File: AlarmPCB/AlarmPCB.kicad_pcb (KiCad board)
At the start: 2 copper layers, 99.9 x 74 mm, 17 parts

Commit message: PCB revisions
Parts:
- moved PB2 13.8 mm to (160.7, 158.0)
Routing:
- net /D3: track 17.0 -> 47.8 mm
- net /D11: track 12.9 -> 43.8 mm
- net /D10: track 13.9 -> 44.8 mm
- net Net-(DS1-Pad9): track 0.00 -> 30.9 mm
- net Net-(DS1-Pad8): track 0.00 -> 30.9 mm
- net Net-(DS1-Pad7): track 0.00 -> 30.9 mm
- net Net-(DS1-Pad3): track 22.6 -> 53.4 mm
- net Net-(DS1-Pad16): track 31.6 -> 62.4 mm
- net Net-(DS1-Pad10): track 0.00 -> 30.9 mm
- net /D5: track 17.0 -> 47.8 mm
- net /D4: track 17.0 -> 47.8 mm
- net /D12: track 15.5 -> 46.3 mm
- net /D2: track 17.0 -> 47.8 mm
- net /A1: track 0.00 -> 19.3 mm
- net /A2: track 19.1 -> 30.1 mm
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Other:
- board text added: "G01_B03"

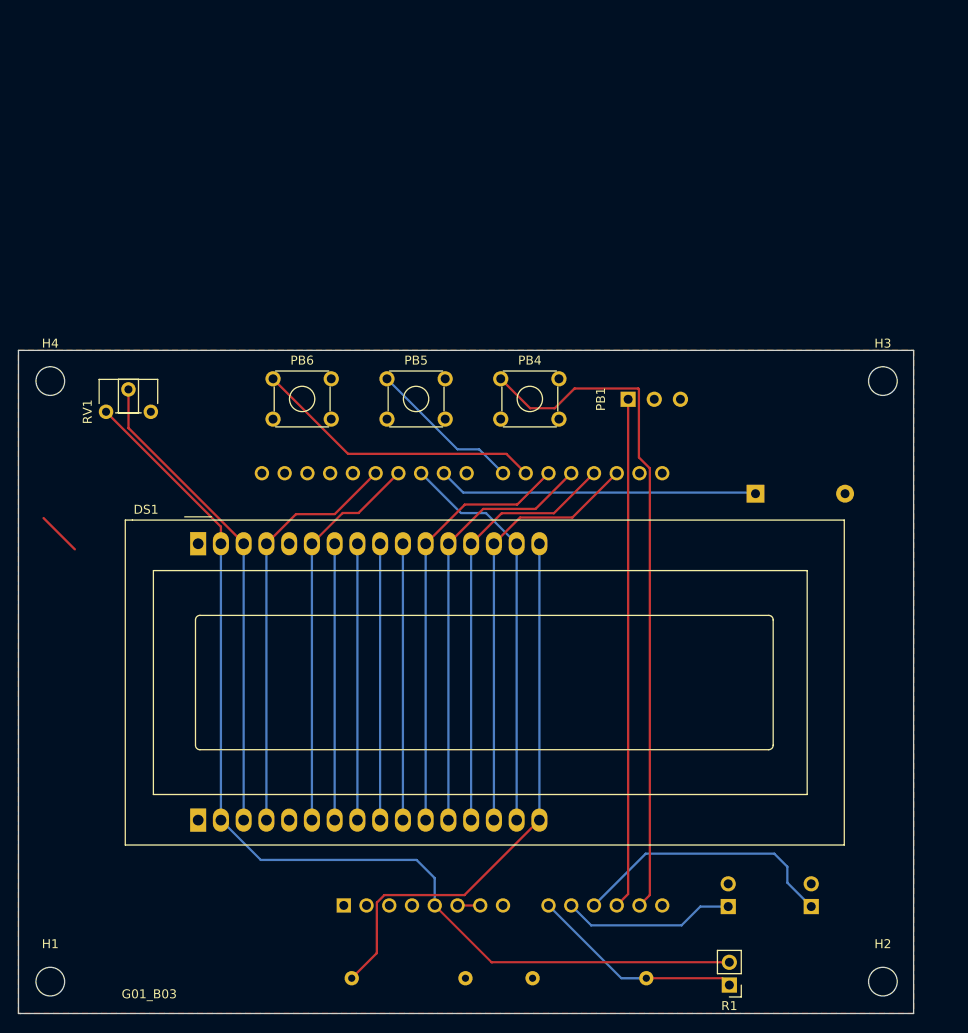
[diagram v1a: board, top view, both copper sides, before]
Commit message: Updated Pot footprint
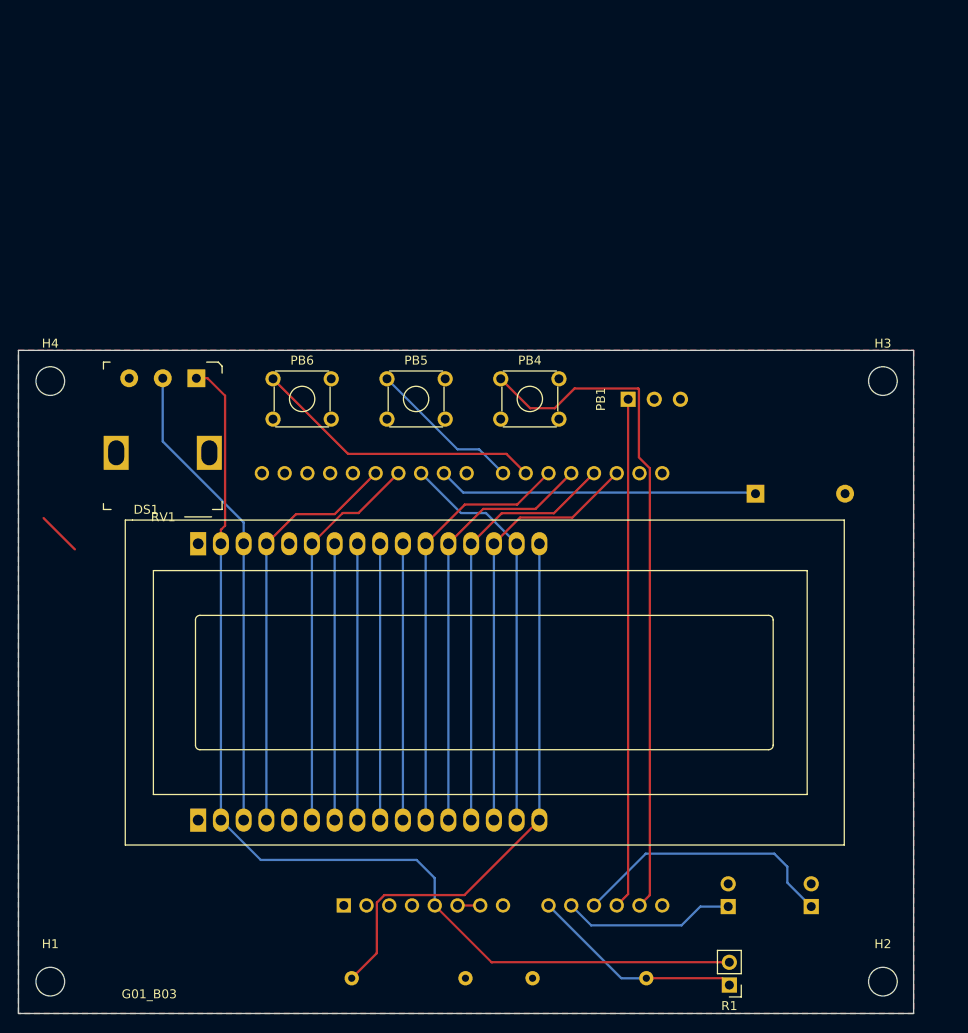
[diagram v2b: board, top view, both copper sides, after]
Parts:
- RV1: footprint Potentiometer_THT:Potentiometer_ACP_CA6-H2,5_Horizontal -> digikey-footprints:Potentiometer_P120PK-Y25BR10K
- moved RV1 10.8 mm to (92.0, 99.0), turned to 180 degrees
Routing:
- net +5V: track 116.0 -> 116.7 mm
- added copper zone on B.Cu, net GND
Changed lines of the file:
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@@
-(kicad_pcb (version 20171130) (host pcbnew "(5.1.6)-1")
+(kicad_pcb (version 20171130) (host pcbnew "(5.1.4)-1")
   (general
     (thickness 1.6)
     (drawings 22)
-    (tracks 86)
+    (tracks 89)
     (zones 0)
     (modules 17)
@@
   (page A4)
   (layers
-    (0 F.Cu signal hide)
+    (0 F.Cu signal)
     (31 B.Cu signal)
     (32 B.Adhes user)
@@
     (add_net "Net-(DS1-Pad9)")
   )
+  (module digikey-footprints:Potentiometer_P120PK-Y25BR10K (layer F.Cu)
+    (at 92 99 180)
+    (fp_text reference RV1 (at 3.7 -15.5) (layer F.SilkS)
+      (effects (font (size 1 1) (thickness 0.15)))
+    )
+    (fp_text value Contrast (at 3.625 2.8) (layer F.Fab)
+      (effects (font (size 1 1) (thickness 0.15)))
+    )
+    (fp_line (start -2.75 -14.525) (end 10.25 -14.525) (layer F.Fab) (width 0.1))
+    (fp_line (start 10.25 -14.525) (end 10.25 1.675) (layer F.Fab) (width 0.1))
+    (fp_line (start -2.75 1.275) (end -2.375 1.675) (layer F.Fab) (width 0.1))
+    (fp_line (start -2.375 1.675) (end 10.25 1.675) (layer F.Fab) (width 0.1))
+    (fp_line (start -2.75 1.275) (end -2.75 -14.525) (layer F.Fab) (width 0.1))
+    (fp_line (start 10.375 -14.65) (end 10.375 -14) (layer F.SilkS) (width 0.1))
+    (fp_line (start 9.525 -14.65) (end 10.375 -14.65) (layer F.SilkS) (width 0.1))
+    (fp_line (start 10.375 1.8) (end 9.625 1.8) (layer F.SilkS) (width 0.1))
+    (fp_line (start 10.375 1.025) (end 10.375 1.8) (layer F.SilkS) (width 0.1))
+    (fp_line (start -2.875 -14.65) (end -2.875 -13.75) (layer F.SilkS) (width 0.1))
+    (fp_line (start -1.8 -14.65) (end -2.875 -14.65) (layer F.SilkS) (width 0.1))
+    (fp_line (start -2.45 1.8) (end -1.15 1.8) (layer F.SilkS) (width 0.1))
+    (fp_line (start -2.875 1.35) (end -2.45 1.8) (layer F.SilkS) (width 0.1))
+    (fp_line (start -2.875 0.575) (end -2.875 1.35) (layer F.SilkS) (width 0.1))
+    (fp_text user %R (at 4.05 -6.65) (layer F.Fab)
+      (effects (font (size 1 1) (thickness 0.15)))
+    )
+    (fp_line (start -3.1 -14.825) (end 10.6 -14.825) (layer F.CrtYd) (width 0.05))
+    (fp_line (start 10.6 -14.825) (end 10.6 1.975) (layer F.CrtYd) (width 0.05))
+    (fp_line (start 10.6 1.975) (end -3.1 1.975) (layer F.CrtYd) (width 0.05))
+    (fp_line (start -3.1 1.975) (end -3.1 -14.825) (layer F.CrtYd) (width 0.05))
+    (pad 4 thru_hole rect (at 8.95 -8.325 180) (size 2.8 3.8) (drill oval 1.8 2.8) (layers *.Cu *.Mask))
+    (pad 4 thru_hole rect (at -1.45 -8.325 180) (size 2.8 3.8) (drill oval 1.8 2.8) (layers *.Cu *.Mask))
+    (pad 3 thru_hole circle (at 7.5 0 180) (size 2 2) (drill 1) (layers *.Cu *.Mask)
+      (net 5 GND))
+    (pad 2 thru_hole circle (at 3.75 0 180) (size 2 2) (drill 1) (layers *.Cu *.Mask)
+      (net 36 "Net-(DS1-Pad3)"))
+    (pad 1 thru_hole rect (at 0 0 180) (size 2 2) (drill 1) (layers *.Cu *.Mask)
+      (net 20 +5V))
+  )
   (module Display:WC1602A (layer F.Cu)
     (at 92.202 117.475)
@@
     )
   )
-  (module Potentiometer_THT:Potentiometer_ACP_CA6-H2,5_Horizontal (layer F.Cu)
-    (at 81.915 102.743 90)
-    (descr "Potentiometer, horizontal, ACP CA6-H2,5, http://www.acptechnologies.com/wp-content/uploads/2017/06/01-ACP-CA6.pdf")
-    (tags "Potentiometer horizontal ACP CA6-H2,5")
-    (fp_text reference RV1 (at 0 -2.06 90) (layer F.SilkS)
-      (effects (font (size 1 1) (thickness 0.15)))
-    )
-    (fp_text value Contrast (at 0 7.06 90) (layer F.Fab)
-      (effects (font (size 1 1) (thickness 0.15)))
-    )
-    (fp_line (start 3.75 -1.1) (end -1.1 -1.1) (layer F.CrtYd) (width 0.05))
-    (fp_line (start 3.75 6.1) (end 3.75 -1.1) (layer F.CrtYd) (width 0.05))
-    (fp_line (start -1.1 6.1) (end 3.75 6.1) (layer F.CrtYd) (width 0.05))
-    (fp_line (start -1.1 -1.1) (end -1.1 6.1) (layer F.CrtYd) (width 0.05))
-    (fp_line (start 3.62 1.38) (end 3.62 3.62) (layer F.SilkS) (width 0.12))
-    (fp_line (start -0.121 1.38) (end -0.121 3.62) (layer F.SilkS) (width 0.12))
-    (fp_line (start -0.121 3.62) (end 3.62 3.62) (layer F.SilkS) (width 0.12))
-    (fp_line (start -0.121 1.38) (end 3.62 1.38) (layer F.SilkS) (width 0.12))
-    (fp_line (start -0.121 1.066) (end -0.121 3.935) (layer F.SilkS) (width 0.12))
-    (fp_line (start 3.62 -0.77) (end 3.62 5.77) (layer F.SilkS) (width 0.12))
-    (fp_line (start 0.925 5.77) (end 3.62 5.77) (layer F.SilkS) (width 0.12))
-    (fp_line (start 0.925 -0.77) (end 3.62 -0.77) (layer F.SilkS) (width 0.12))
-    (fp_line (start 3.5 1.5) (end 0 1.5) (layer F.Fab) (width 0.1))
-    (fp_line (start 3.5 3.5) (end 3.5 1.5) (layer F.Fab) (width 0.1))
-    (fp_line (start 0 3.5) (end 3.5 3.5) (layer F.Fab) (width 0.1))
-    (fp_line (start 0 1.5) (end 0 3.5) (layer F.Fab) (width 0.1))
-    (fp_line (start 0 -0.65) (end 3.5 -0.65) (layer F.Fab) (width 0.1))
-    (fp_line (start 0 5.65) (end 0 -0.65) (layer F.Fab) (width 0.1))
-    (fp_line (start 3.5 5.65) (end 0 5.65) (layer F.Fab) (width 0.1))
-    (fp_line (start 3.5 -0.65) (end 3.5 5.65) (layer F.Fab) (width 0.1))
-    (fp_text user %R (at 1.75 2.5 90) (layer F.Fab)
-      (effects (font (size 0.78 0.78) (thickness 0.15)))
-    )
-    (pad 1 thru_hole circle (at 0 0 90) (size 1.62 1.62) (drill 0.9) (layers *.Cu *.Mask)
-      (net 20 +5V))
-    (pad 2 thru_hole circle (at 2.5 2.5 90) (size 1.62 1.62) (drill 0.9) (layers *.Cu *.Mask)
-      (net 36 "Net-(DS1-Pad3)"))
-    (pad 3 thru_hole circle (at 0 5 90) (size 1.62 1.62) (drill 0.9) (layers *.Cu *.Mask)
-      (net 5 GND))
-    (model ${KISYS3DMOD}/Potentiometer_THT.3dshapes/Potentiometer_ACP_CA6-H2,5_Horizontal.wrl
-      (at (xyz 0 0 0))
-      (scale (xyz 1 1 1))
-      (rotate (xyz 0 0 0))
-    )
-  )
   (module Resistor_THT:R_Axial_DIN0309_L9.0mm_D3.2mm_P12.70mm_Horizontal (layer B.Cu)
     (at 129.54 165.989)
@@
   (segment (start 126.619 107.442) (end 128.778 109.601) (width 0.254) (layer F.Cu) (net 19))
   (segment (start 108.943 107.442) (end 126.619 107.442) (width 0.254) (layer F.Cu) (net 19))
-  (segment (start 94.742 115.57) (end 94.742 117.475) (width 0.254) (layer F.Cu) (net 20))
-  (segment (start 81.915 102.743) (end 94.742 115.57) (width 0.254) (layer F.Cu) (net 20))
   (segment (start 124.968 164.211) (end 151.511 164.211) (width 0.254) (layer F.Cu) (net 20))
   (segment (start 118.618 157.861) (end 124.968 164.211) (width 0.254) (layer F.Cu) (net 20))
@@
   (segment (start 99.187 152.781) (end 94.742 148.336) (width 0.254) (layer B.Cu) (net 20))
   (segment (start 116.586 152.781) (end 99.187 152.781) (width 0.254) (layer B.Cu) (net 20))
+  (segment (start 94.742 115.921) (end 94.742 117.475) (width 0.254) (layer F.Cu) (net 20))
+  (segment (start 95.205601 115.457399) (end 94.742 115.921) (width 0.254) (layer F.Cu) (net 20))
+  (segment (start 95.205601 100.951601) (end 95.205601 115.457399) (width 0.254) (layer F.Cu) (net 20))
+  (segment (start 93.254 99) (end 95.205601 100.951601) (width 0.254) (layer F.Cu) (net 20))
+  (segment (start 92 99) (end 93.254 99) (width 0.254) (layer F.Cu) (net 20))
   (segment (start 121.97083 113.10617) (end 117.602 117.475) (width 0.254) (layer F.Cu) (net 21))
   (segment (start 127.81283 113.10617) (end 121.97083 113.10617) (width 0.254) (layer F.Cu) (net 21))
@@
   (segment (start 109.982 117.475) (end 109.982 148.336) (width 0.254) (layer B.Cu) (net 34))
   (segment (start 107.442 117.475) (end 107.442 148.336) (width 0.254) (layer B.Cu) (net 35))
-  (segment (start 97.282 117.427488) (end 97.282 117.475) (width 0.254) (layer F.Cu) (net 36))
-  (segment (start 84.415 104.560488) (end 97.282 117.427488) (width 0.254) (layer F.Cu) (net 36))
-  (segment (start 84.415 100.243) (end 84.415 104.560488) (width 0.254) (layer F.Cu) (net 36))
   (segment (start 97.282 117.475) (end 97.282 148.336) (width 0.254) (layer B.Cu) (net 36))
+  (segment (start 97.282 115.097082) (end 97.282 117.475) (width 0.254) (layer B.Cu) (net 36))
+  (segment (start 88.25 99) (end 88.25 106.065082) (width 0.254) (layer B.Cu) (net 36))
+  (segment (start 88.25 106.065082) (end 97.282 115.097082) (width 0.254) (layer B.Cu) (net 36))
   (zone (net 5) (net_name GND) (layer F.Cu) (hatch edge 0.508)
     (connect_pads (clearance 0.508))
     (min_thickness 0.254)
+    (fill yes (arc_segments 32) (thermal_gap 0.508) (thermal_bridge_width 0.508))
+    (polygon
+      (pts
+        (xy 172.085 169.926) (xy 72.136 169.926) (xy 72.136 95.885) (xy 172.085 95.885)
+      )
+    )
+  )
+  (zone (net 5) (net_name GND) (layer B.Cu) (hatch edge 0.508)
+    (connect_pads (clearance 0.508))
+    (min_thickness 0.254)

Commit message: PCB rev
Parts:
- PB1: footprint Connector_PinHeader_2.54mm:PinHeader_1x03_P2.54mm_Vertical -> Button_Switch_THT:SW_TH_Tactile_Omron_B3F-10xx
- moved PB1 4.90 mm to (145.3, 103.7), turned to 180 degrees
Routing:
- net /A4: track 76.4 -> 68.8 mm
- net GND: track 7.49 -> 2.54 mm
- net /A3: track 57.0 -> 60.3 mm

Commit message: Final PCB
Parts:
- moved A1 20.2 mm to (88.4, 160.6)
- moved PB2 14.4 mm to (146.3, 157.7)
- moved PB3 14.4 mm to (137.0, 157.7)
- moved RV1 9.69 mm to (82.3, 98.1), turned to 270 degrees
- moved H3 1.43 mm to (168.1, 98.0)
- moved H4 1.38 mm to (76.1, 98.0)
- moved PB1 1.12 mm to (146.3, 103.2)
- moved PB4 0.92 mm to (126.8, 98.8)
- moved H2 0.67 mm to (168.1, 166.0)
- moved PB5 0.65 mm to (113.8, 98.8)
- moved H1 0.55 mm to (76.1, 166.0)
- moved PB6 0.42 mm to (100.8, 98.8)
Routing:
- net Net-(A1-Pad24): track 35.7 -> 56.0 mm
- net /D10: track 44.8 -> 63.7 mm
- net Net-(A1-Pad9): track 23.9 -> 42.8 mm
- net /D6: track 32.6 -> 16.8 mm
- net +5V: track 116.7 -> 129.7 mm
- net /A3: track 60.3 -> 71.3 mm
- net /D5: track 47.8 -> 39.3 mm
- net /D4: track 47.8 -> 39.3 mm
- net /D3: track 47.8 -> 39.3 mm
- net /D2: track 47.8 -> 39.3 mm
- net /A1: track 19.3 -> 25.7 mm
- net /D12: track 46.3 -> 40.8 mm
- net /A4: track 68.8 -> 64.8 mm, vias 0 -> 1
- net Net-(DS1-Pad3): track 53.1 -> 56.8 mm
- net /A2: track 30.1 -> 32.9 mm
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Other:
- board size 99.9 x 74 mm -> 100 x 76 mm

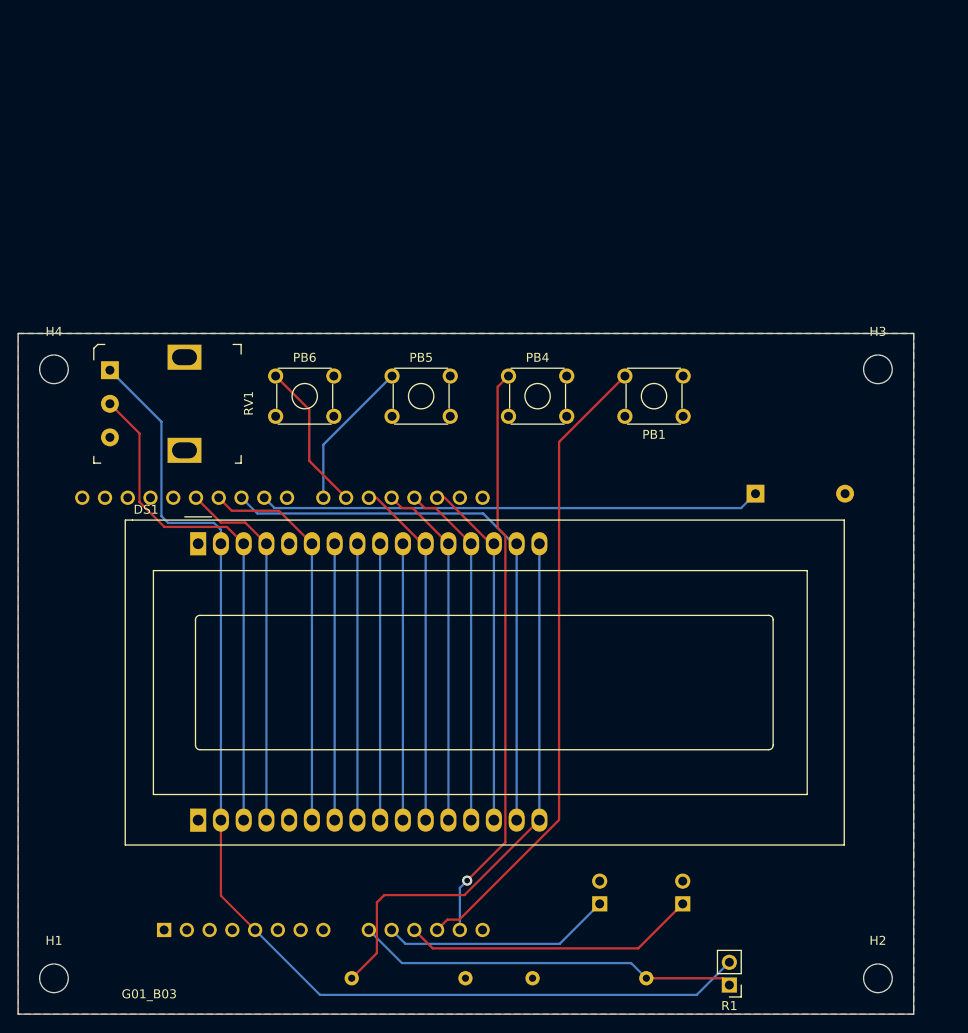
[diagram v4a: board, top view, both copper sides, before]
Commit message: Fixed Short
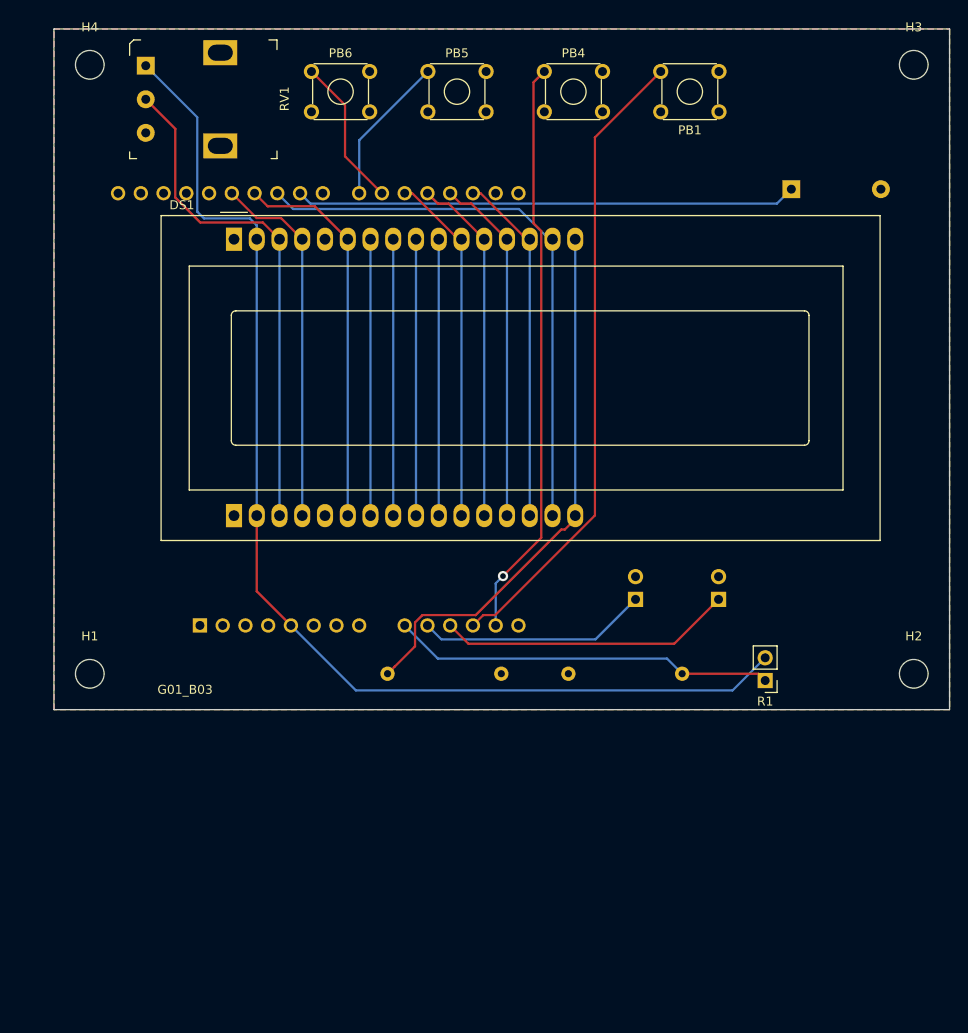
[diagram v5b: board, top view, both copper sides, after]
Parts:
- moved A1 34.2 mm to (92.4, 126.6)
- moved BZ1 34.2 mm to (158.4, 77.9)
- moved DS1 34.2 mm to (96.2, 83.5)
- moved H1 34.2 mm to (80.1, 132.0)
- moved H2 34.2 mm to (172.1, 132.0)
- moved H3 34.2 mm to (172.1, 64.0)
- moved H4 34.2 mm to (80.1, 64.0)
- moved PB1 34.2 mm to (150.3, 69.2)
- moved PB4 34.2 mm to (130.8, 64.8)
- moved PB5 34.2 mm to (117.8, 64.8)
- moved PB6 34.2 mm to (104.8, 64.8)
- moved R1 34.2 mm to (155.5, 132.8)
- moved R2 34.2 mm to (133.5, 132.0)
- moved R3 34.2 mm to (113.3, 132.0)
- moved RV1 34.2 mm to (86.3, 64.1)
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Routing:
- net Net-(DS1-Pad16): track 62.4 -> 60.9 mm
